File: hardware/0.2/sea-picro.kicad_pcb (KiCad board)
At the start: 4 copper layers, 17.8 x 33 mm, 56 parts, among them J1 USB_C_Receptacle_USB2.0, J2 0.1" x 12, J3 0.1" x 12, Q1 FDG6335N, Q2 FDG6335N, SW1 RESET, U1 AP2112K-3.3, U3 W25Q128JVPIQ, U4 RP2040, Y1 12MHz

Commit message: 0.2 ready for review
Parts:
- removed the U3 at (126.3, 89.3)
- added LOGO2: Sea-Picro, josh-logos:sea-picro-silk, B.Cu at (126.2, 89.9)
- added R6: 5K1, Resistor_SMD:R_0402_1005Metric, F.Cu at (122.4, 92.2)
- added U2: GD25Q64CWIGR, Package_SON:WSON-8-1EP_6x5mm_P1.27mm_EP3.4x4.3mm, F.Cu at (126.3, 89.3)
- Q1, Q2: value FDG6335N -> 2N7002DW-7-F
- R10: value 10K -> 5K1
- U1: value AP2112K-3.3 -> ME6211C33M5G-N
- moved R10 2.37 mm to (122.4, 90.2), turned to 90 degrees
- moved C15 0.74 mm to (121.2, 94.2)
- moved D1 0.35 mm to (121.5, 87.7)
- moved D2 0.32 mm to (121.1, 90.8)
- moved R3 0.30 mm to (120.9, 85.1)
- moved D3 0.10 mm to (131.4, 84.7)
- renumbered U4 to U3
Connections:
- R10 pad 1: +3V3 -> Net-(R10-Pad1)
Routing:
- net /FLASH_nCS: track 20.5 -> 22.5 mm
- net /23_MOSI: track 12.1 -> 10.6 mm, vias 0 -> 1
- net +3V3: track 39.1 -> 37.7 mm, vias 12 -> 13
- net Net-(R10-Pad1): track 0.00 -> 0.88 mm
- net +5V: track 24.9 -> 24.4 mm
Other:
- board text added: "<- VScore along -> these edges if panelising"

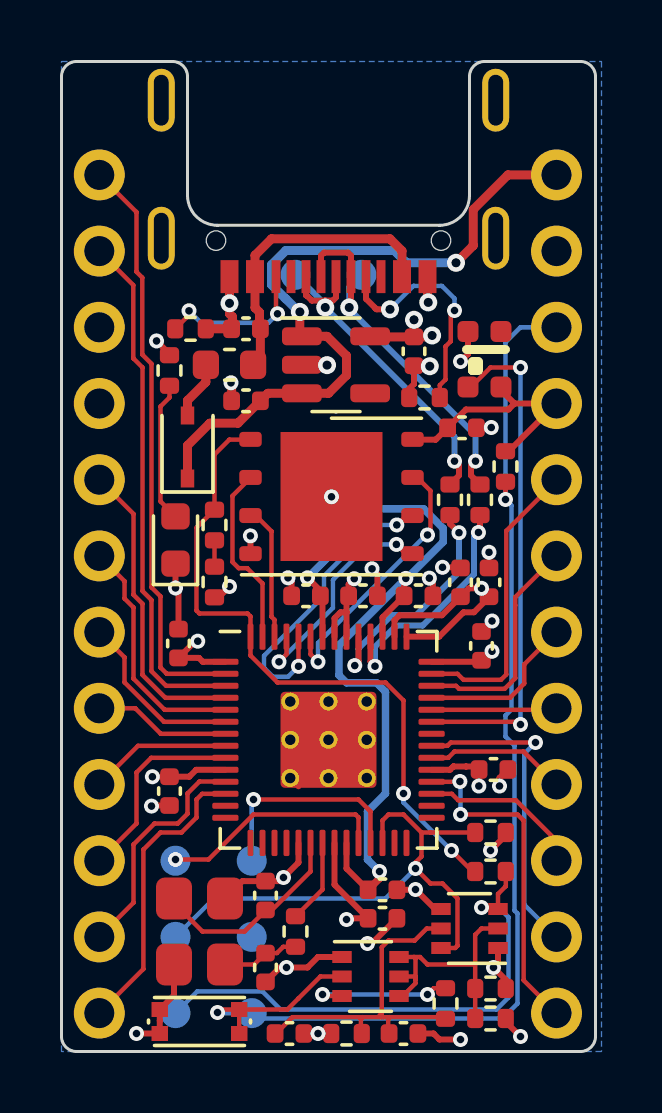
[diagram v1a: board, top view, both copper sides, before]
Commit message: add USB D+- on pin header
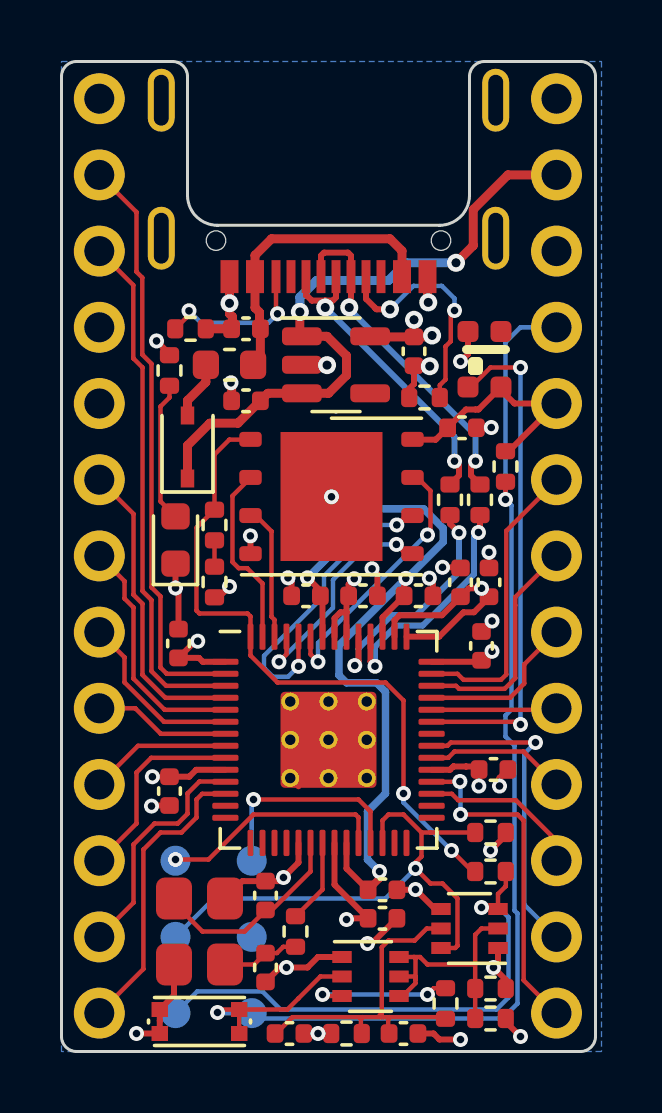
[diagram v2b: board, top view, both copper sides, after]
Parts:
- removed TP1: -, TestPoint:TestPoint_Pad_D1.0mm
- removed TP2: +, TestPoint:TestPoint_Pad_D1.0mm
- added J4: D+, josh-connectors:PinHeader_1x01_Circle, F.Cu at (118.6, 76.0)
- added J5: D-, josh-connectors:PinHeader_1x01_Circle, F.Cu at (133.8, 76.0)
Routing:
- net /USB+: track 12.0 -> 23.6 mm
- net /USB-: track 12.6 -> 23.7 mm
- net +5V: track 24.4 -> 22.1 mm
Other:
- board text added: "5V"
- board text added: "D+"
- board text added: "D-"
- board text removed: "+"
- board text removed: "-"
- board text removed: "US"
- board text removed: "VB"
